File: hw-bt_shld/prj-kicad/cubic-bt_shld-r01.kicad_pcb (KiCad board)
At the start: 2 copper layers, 13.3 x 24.5 mm, 2 parts

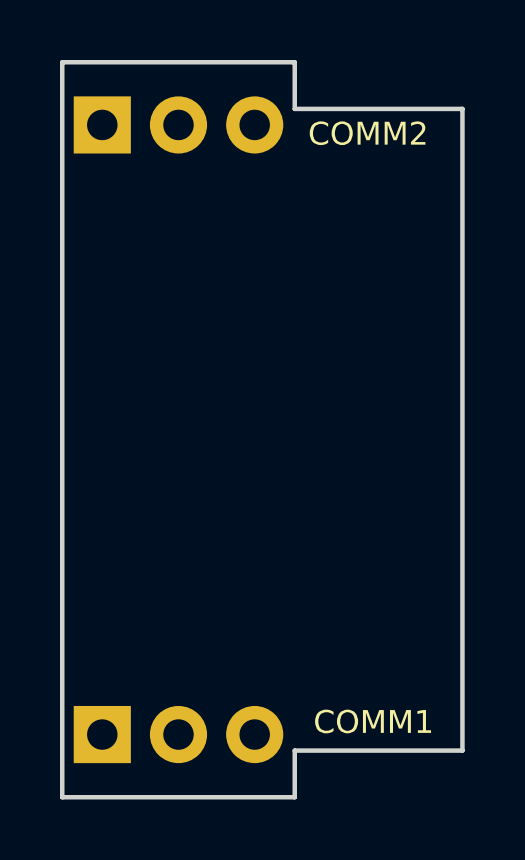
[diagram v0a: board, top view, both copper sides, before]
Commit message: = UPD: Insert CC2540 and the HF interface to antenna
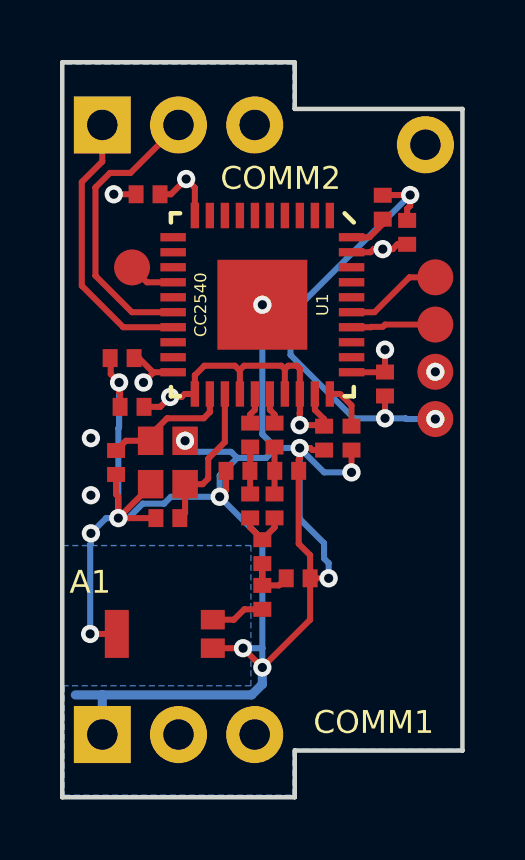
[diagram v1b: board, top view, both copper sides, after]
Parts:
- added A1: SMD_ANTENNA, ANT_BT_W3008, F.Cu at (145.7, 94.1)
- added C1: 18pF, SMD0402, F.Cu at (148.5, 87.4)
- added C10: 1uF, SMD0402, F.Cu at (152.9, 79.8)
- added C11: 100nF, SMD0402, F.Cu at (153.7, 80.7)
- added C12: 100nF, SMD0402, F.Cu at (153.0, 85.7)
- added C13: 100nF, SMD0402, F.Cu at (151.0, 87.5)
- added C14: 100nF, SMD0402, F.Cu at (144.6, 86.5)
- added C15: 100nF, SMD0402, F.Cu at (145.1, 79.4)
- added C17: 1nF, SMD0402, F.Cu at (144.2, 84.9)
- added C2: 18pF, SMD0402, F.Cu at (149.3, 87.4)
- added C3: 1pF, SMD0402, F.Cu at (149.7, 88.6)
- added C4: 1pF, SMD0402, F.Cu at (148.5, 89.8)
- added C5: 1pF, SMD0402, F.Cu at (150.1, 92.2)
- added C8: 12pF, SMD0402, F.Cu at (144.0, 88.3)
- added C9: 12pF, SMD0402, F.Cu at (145.8, 90.2)
- added L1: 2nH, SMD0402, F.Cu at (148.1, 88.6)
- added L2: 2nH, SMD0402, F.Cu at (149.3, 89.8)
- added L3: 1nH, SMD0402, F.Cu at (148.9, 91.3)
- added L4: 3nH, SMD0402, F.Cu at (148.9, 92.8)
- added P1: CONN_1, TP_SMD, F.Cu at (154.7, 86.9)
- added P101: CONN_1, TP_SMD, F.Cu at (144.6, 81.8)
- added P2: CONN_1, TP_SMD, F.Cu at (154.7, 85.3)
- added P3: CONN_1, TP_SMD, F.Cu at (154.7, 82.2)
- added P4: CONN_1, TP_SMD, F.Cu at (154.7, 83.7)
- added PWR1: CONN_1, TP_PIN, F.Cu at (154.4, 77.7)
- added R1: 56k, SMD0402, F.Cu at (151.9, 87.5)
- added U1: CC2540, QFN40, F.Cu at (148.9, 83.1)
- added X1: 32MHz, OSC_FA128, F.Cu at (145.8, 88.3)
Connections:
- net N-000006 renamed INT
- COMM1 pad 1: N-000001 -> GND
- COMM2 pad 1: N-000004 -> UART_RX
- COMM2 pad 2: N-000005 -> UART_TX
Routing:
- net GND: track 0.00 -> 105.3 mm, vias 0 -> 18
- net +VDD: track 0.00 -> 42.2 mm, vias 0 -> 5
- net Reset: track 0.00 -> 11.8 mm, vias 0 -> 2
- net UART_TX: track 0.00 -> 9.67 mm
- net UART_RX: track 0.00 -> 9.26 mm
- net N-0000011: track 0.00 -> 5.10 mm
- net N-0000013: track 0.00 -> 4.38 mm
- net DBG_DD: track 0.00 -> 3.27 mm
- net DBG_DC: track 0.00 -> 2.83 mm
- net N-0000042: track 0.00 -> 1.79 mm
- net N-0000039: track 0.00 -> 1.79 mm
- net N-0000038: track 0.00 -> 1.62 mm
- net N-000004: track 0.00 -> 1.57 mm
- net N-0000012: track 0.00 -> 1.57 mm
- net N-0000041: track 0.00 -> 1.57 mm
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- added copper zone on Inner1, net +VDD
- added copper zone on B.Cu, net GND
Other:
- copper layers 2 -> 4
- net class Default: trace_width 0.254 -> 0.1524
- rule pad_to_mask_clearance: 0.2 -> 0.254
- rule via_min_drill: 0.3048 -> 0.20066
- rule via_min_size: 0.7112 -> 0.50038
